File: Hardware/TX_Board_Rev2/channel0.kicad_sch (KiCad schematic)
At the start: 65 parts, among them IC15 PMA3-63GLN+, IC19 PE42423B-Z, IC23 PE42423B-Z, IC4 MAPS-010164-TR0500, IC5 QPA9122TR7, J3 MM8030-2610RJ3, J4 Conn_Coaxial, J5 Conn_Coaxial

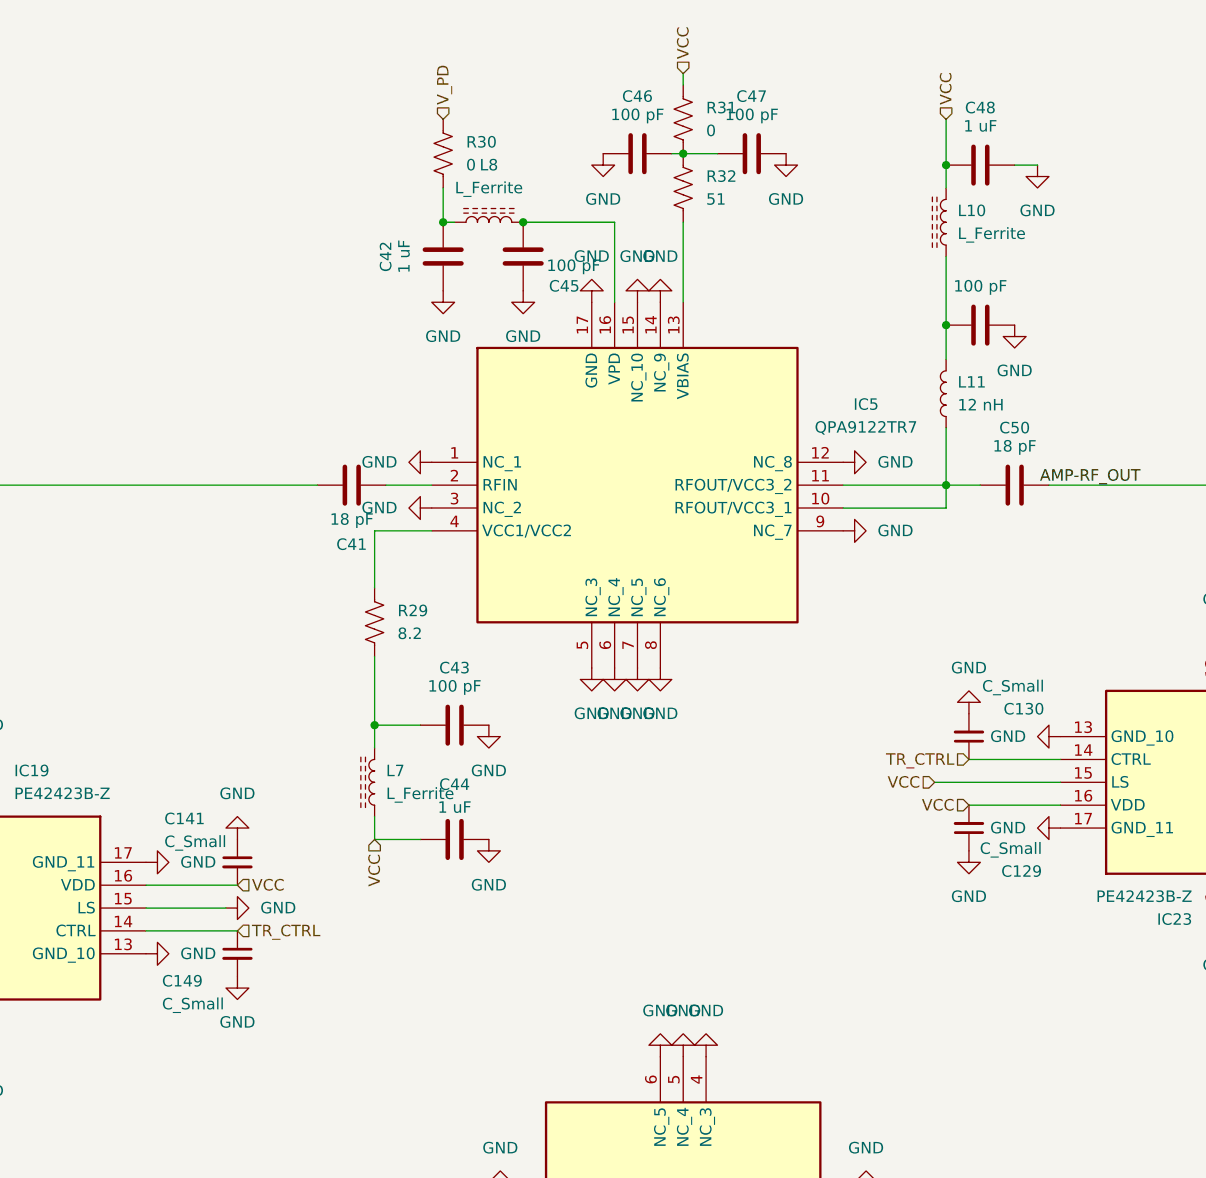
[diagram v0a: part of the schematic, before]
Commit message: Rev2 layout partially complete
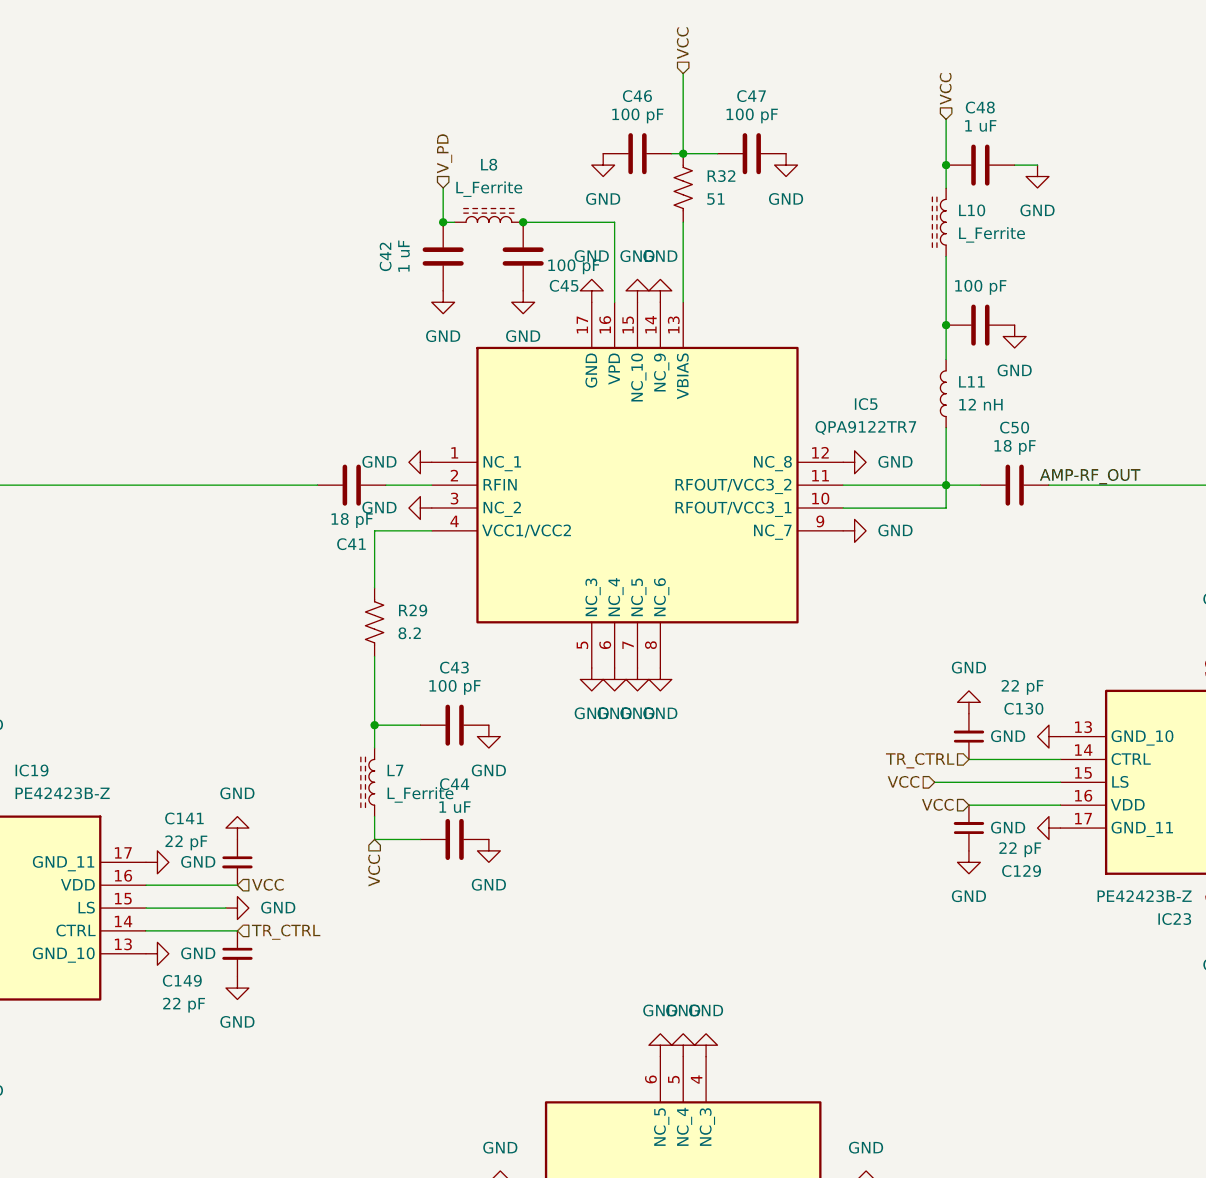
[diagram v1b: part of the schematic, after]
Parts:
- removed R30, R31: 0, Resistor_SMD:R_0603_1608Metric, symbol tx_board_symbol_library:R_US
- AT2: footprint tx_board_footprints:QFN50P300X300X90-17N -> RFSA3713:QFN50P300X300X90-17N
- C1, C10, C11, C12, C2, C3, C36, C37, C38, C39, C40, C42, C43, C44, C45, C46, C47, C48, C49, C6, C7, C8, C9: footprint Capacitor_SMD:C_0603_1608Metric -> Capacitor_SMD:C_0402_1005Metric
- C113, C116: footprint Capacitor_SMD:C_0402_1005Metric_Pad0.74x0.62mm_HandSolder -> Capacitor_SMD:C_0402_1005Metric
- C114: footprint Capacitor_SMD:C_1206_3216Metric_Pad1.33x1.80mm_HandSolder -> Capacitor_SMD:C_0402_1005Metric
- C115: footprint Capacitor_SMD:C_0603_1608Metric_Pad1.08x0.95mm_HandSolder -> Capacitor_SMD:C_0402_1005Metric
- C129, C130, C141, C149: value C_Small -> 22 pF; footprint (none) -> Capacitor_SMD:C_0402_1005Metric
- IC19, IC23: footprint PE42423B-Z:QFN50P300X300X90-17N-D -> PE42423:QFN50P300X300X90-17N-D
- IC4: footprint tx_board_footprints:QFN50P400X400X100-25N-D -> MAPS-010164-TR0500:QFN50P400X400X100-25N-D
- IC5: footprint tx_board_footprints:QPA9122TR7 -> QPA9122-TR7:QPA9122TR7
- J3: footprint tx_board_footprints:MM80302610RJ3 -> MM8030-2610RJ3:MM80302610RJ3
- R12, R13, R14, R15, R16, R17, R29, R32, R4: footprint Resistor_SMD:R_0603_1608Metric -> Resistor_SMD:R_0402_1005Metric
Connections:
- net VCC: now also C46.2, C47.1, R32.1
- net V_PD: now also C42.2, L8.1

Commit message: Rev2 Complete
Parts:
- removed J4: Conn_Coaxial, Connector_Coaxial:SMA_Samtec_SMA-J-P-H-ST-EM1_EdgeMount, symbol Connector:Conn_Coaxial
- added J1: CONSMA022-G, CONSMA022_G:LINX_CONSMA022-G, symbol CONSMA022-G:CONSMA022-G
- added R51, R52: 20k, Resistor_SMD:R_0402_1005Metric, symbol Device:R_US
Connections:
- net GND: now also J1.2, J1.3, J1.4, J1.5, R51.2; no longer IC19.15 (LS)
- net OUTPUT: now also J1.1
- net VCC: now also R52.1; no longer IC23.15 (LS)
- new net: IC23.15 (LS), R52.2
- new net: IC19.15 (LS), R51.1

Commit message: Rev 3, rotated interface connectors
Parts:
- renumbered AT2 to AT0, HY2 to CPL0, J5 to CPL_PORT0, J1 to J0, J3 to J8, IC15 to LNA0, IC5 to PA0, IC4 to PS0, IC19 to SW00, IC23 to SW01
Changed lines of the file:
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@@
 		(dnp no)
 		(fields_autoplaced yes)
-		(property "Reference" "J1"
+		(property "Reference" "J0"
 			(at 673.2905 262.89 0)
 			(effects
@@
 			(project ""
 				(path "/5327d041-dca0-47c6-802d-ce81714adf6c/7bb8dd1e-0839-4907-9be8-cd94b974a535"
-					(reference "J1")
+					(reference "J0")
 					(unit 1)
 				)
@@
 		(dnp no)
 		(fields_autoplaced yes)
-		(property "Reference" "IC23"
+		(property "Reference" "SW01"
 			(at 558.2219 266.7 90)
 			(effects
@@
 			(project "TX_Board_Rev2"
 				(path "/5327d041-dca0-47c6-802d-ce81714adf6c/7bb8dd1e-0839-4907-9be8-cd94b974a535"
-					(reference "IC23")
+					(reference "SW01")
 					(unit 1)
 				)
@@
 		(on_board yes)
 		(dnp no)
-		(property "Reference" "IC15"
+		(property "Reference" "LNA0"
 			(at 502.412 303.276 0)
 			(effects
@@
 			(project "TX_Board_Rev2"
 				(path "/5327d041-dca0-47c6-802d-ce81714adf6c/7bb8dd1e-0839-4907-9be8-cd94b974a535"
-					(reference "IC15")
+					(reference "LNA0")
 					(unit 1)
 				)
@@
 		(on_board yes)
 		(dnp no)
-		(property "Reference" "IC4"
+		(property "Reference" "PS0"
 			(at 250.19 248.8498 0)
 			(effects
@@
 			(project "TX_Board_Rev2"
 				(path "/5327d041-dca0-47c6-802d-ce81714adf6c/7bb8dd1e-0839-4907-9be8-cd94b974a535"
-					(reference "IC4")
+					(reference "PS0")
 					(unit 1)
 				)
@@
 		(on_board yes)
 		(dnp no)
-		(property "Reference" "J3"
+		(property "Reference" "J8"
 			(at 381.762 286.766 90)
 			(effects
@@
 			(project "TX_Board_Rev2"
 				(path "/5327d041-dca0-47c6-802d-ce81714adf6c/7bb8dd1e-0839-4907-9be8-cd94b974a535"
-					(reference "J3")
+					(reference "J8")
 					(unit 1)
 				)
@@
 		(dnp no)
 		(fields_autoplaced yes)
-		(property "Reference" "IC5"
+		(property "Reference" "PA0"
 			(at 521.97 209.4798 0)
 			(effects
@@
 			(project "TX_Board_Rev2"
 				(path "/5327d041-dca0-47c6-802d-ce81714adf6c/7bb8dd1e-0839-4907-9be8-cd94b974a535"
-					(reference "IC5")
+					(reference "PA0")
 					(unit 1)
 				)
@@
 		(dnp no)
 		(fields_autoplaced yes)
-		(property "Reference" "HY2"
+		(property "Reference" "CPL0"
 			(at 641.35 243.84 0)
 			(effects
@@
 			(project "TX_Board_Rev2"
 				(path "/5327d041-dca0-47c6-802d-ce81714adf6c/7bb8dd1e-0839-4907-9be8-cd94b974a535"
-					(reference "HY2")
+					(reference "CPL0")
 					(unit 1)
 				)
@@
 		(dnp no)
 		(fields_autoplaced yes)
-		(property "Reference" "IC19"
+		(property "Reference" "SW00"
 			(at 427.2981 250.19 90)
 			(effects
@@
 			(project "TX_Board_Rev2"
 				(path "/5327d041-dca0-47c6-802d-ce81714adf6c/7bb8dd1e-0839-4907-9be8-cd94b974a535"
-					(reference "IC19")
+					(reference "SW00")
 					(unit 1)
 				)
@@
 		(dnp no)
 		(fields_autoplaced yes)
-		(property "Reference" "J5"
+		(property "Reference" "CPL_PORT0"
 			(at 690.88 241.5931 0)
 			(effects
@@
 			(project "TX_Board_Rev2"
 				(path "/5327d041-dca0-47c6-802d-ce81714adf6c/7bb8dd1e-0839-4907-9be8-cd94b974a535"
-					(reference "J5")
+					(reference "CPL_PORT0")
 					(unit 1)
 				)
@@
 		(dnp no)
 		(fields_autoplaced yes)
-		(property "Reference" "AT2"
+		(property "Reference" "AT0"
 			(at 334.01 251.3898 0)
 			(effects
@@
 			(project "TX_Board_Rev2"
 				(path "/5327d041-dca0-47c6-802d-ce81714adf6c/7bb8dd1e-0839-4907-9be8-cd94b974a535"
-					(reference "AT2")
+					(reference "AT0")
 					(unit 1)
 				)

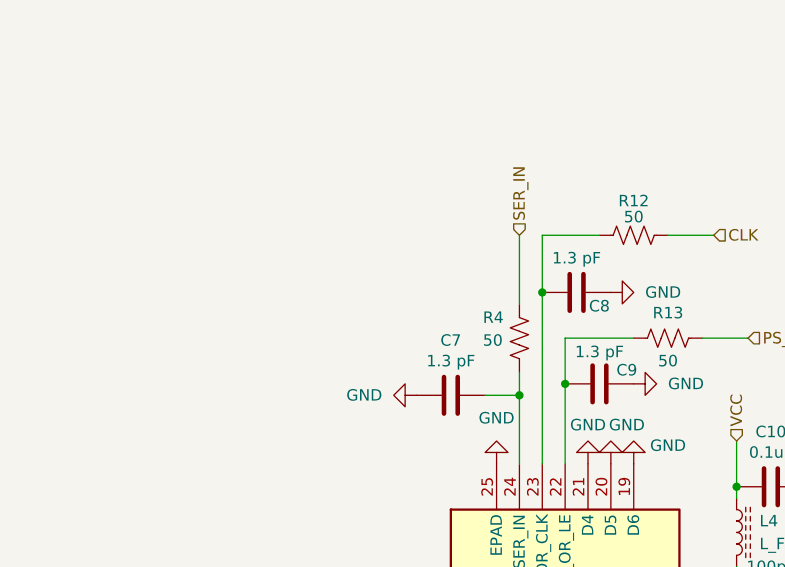
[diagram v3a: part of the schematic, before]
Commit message: optimal radiation patterns + a few rev 3 fixes
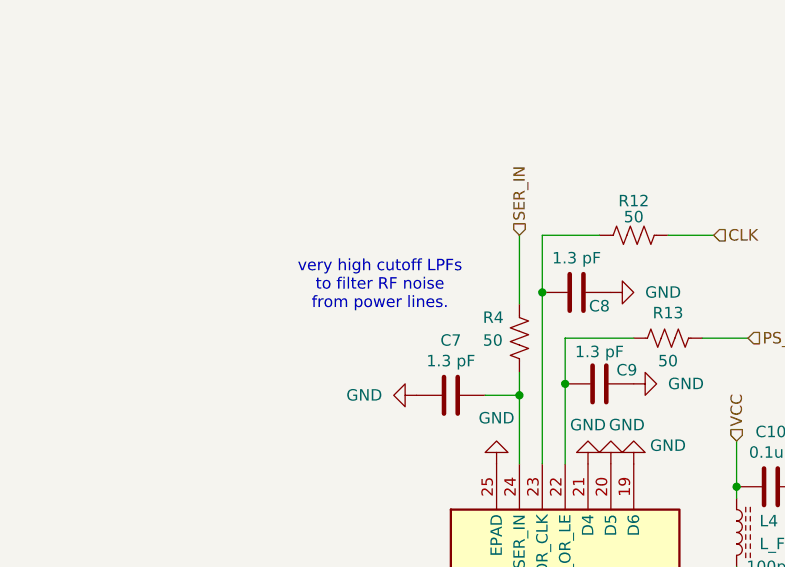
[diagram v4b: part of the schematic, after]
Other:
- note added: "very high cutoff LPFs to filter RF noise from power lines."
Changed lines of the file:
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@@
+		)
+	)
+	(text "very high cutoff LPFs \nto filter RF noise \nfrom power lines."
+		(exclude_from_sim no)
+		(at 206.756 210.058 0)
+		(effects
+			(font
+				(size 1.27 1.27)
+			)
 		)
 	)

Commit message: Restored broken Rev 2 for posterity and cleaned up naming
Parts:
- renumbered AT0 to AT2, CPL0 to HY2, LNA0 to IC15, SW00 to IC19, SW01 to IC23, PS0 to IC4, PA0 to IC5, J0 to J1, J8 to J3, CPL_PORT0 to J5
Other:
- note removed: "very high cutoff LPFs to filter RF noise from power lines."
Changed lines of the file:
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@@
 		)
 	)
-	(text "very high cutoff LPFs \nto filter RF noise \nfrom power lines."
-		(exclude_from_sim no)
-		(at 206.756 210.058 0)
-		(effects
-			(font
-				(size 1.27 1.27)
-			)
-		)
-	)
 	(junction
 		(at 191.77 255.27)
@@
 		(dnp no)
 		(fields_autoplaced yes)
-		(property "Reference" "J0"
+		(property "Reference" "J1"
 			(at 673.2905 262.89 0)
 			(effects
@@
 			(project ""
 				(path "/5327d041-dca0-47c6-802d-ce81714adf6c/7bb8dd1e-0839-4907-9be8-cd94b974a535"
-					(reference "J0")
+					(reference "J1")
 					(unit 1)
 				)
@@
 		(dnp no)
 		(fields_autoplaced yes)
-		(property "Reference" "SW01"
+		(property "Reference" "IC23"
 			(at 558.2219 266.7 90)
 			(effects
@@
 			(project "TX_Board_Rev2"
 				(path "/5327d041-dca0-47c6-802d-ce81714adf6c/7bb8dd1e-0839-4907-9be8-cd94b974a535"
-					(reference "SW01")
+					(reference "IC23")
 					(unit 1)
 				)
@@
 		(on_board yes)
 		(dnp no)
-		(property "Reference" "LNA0"
+		(property "Reference" "IC15"
 			(at 502.412 303.276 0)
 			(effects
@@
 			(project "TX_Board_Rev2"
 				(path "/5327d041-dca0-47c6-802d-ce81714adf6c/7bb8dd1e-0839-4907-9be8-cd94b974a535"
-					(reference "LNA0")
+					(reference "IC15")
 					(unit 1)
 				)
@@
 		(on_board yes)
 		(dnp no)
-		(property "Reference" "PS0"
+		(property "Reference" "IC4"
 			(at 250.19 248.8498 0)
 			(effects
@@
 			(project "TX_Board_Rev2"
 				(path "/5327d041-dca0-47c6-802d-ce81714adf6c/7bb8dd1e-0839-4907-9be8-cd94b974a535"
-					(reference "PS0")
+					(reference "IC4")
 					(unit 1)
 				)
@@
 		(on_board yes)
 		(dnp no)
-		(property "Reference" "J8"
+		(property "Reference" "J3"
 			(at 381.762 286.766 90)
 			(effects
@@
 			(project "TX_Board_Rev2"
 				(path "/5327d041-dca0-47c6-802d-ce81714adf6c/7bb8dd1e-0839-4907-9be8-cd94b974a535"
-					(reference "J8")
+					(reference "J3")
 					(unit 1)
 				)
@@
 		(dnp no)
 		(fields_autoplaced yes)
-		(property "Reference" "PA0"
+		(property "Reference" "IC5"
 			(at 521.97 209.4798 0)
 			(effects
@@
 			(project "TX_Board_Rev2"
 				(path "/5327d041-dca0-47c6-802d-ce81714adf6c/7bb8dd1e-0839-4907-9be8-cd94b974a535"
-					(reference "PA0")
+					(reference "IC5")
 					(unit 1)
 				)
@@
 		(dnp no)
 		(fields_autoplaced yes)
-		(property "Reference" "CPL0"
+		(property "Reference" "HY2"
 			(at 641.35 243.84 0)
 			(effects
@@
 			(project "TX_Board_Rev2"
 				(path "/5327d041-dca0-47c6-802d-ce81714adf6c/7bb8dd1e-0839-4907-9be8-cd94b974a535"
-					(reference "CPL0")
+					(reference "HY2")
 					(unit 1)
 				)
@@
 		(dnp no)
 		(fields_autoplaced yes)
-		(property "Reference" "SW00"
+		(property "Reference" "IC19"
 			(at 427.2981 250.19 90)
 			(effects
@@
 			(project "TX_Board_Rev2"
 				(path "/5327d041-dca0-47c6-802d-ce81714adf6c/7bb8dd1e-0839-4907-9be8-cd94b974a535"
-					(reference "SW00")
+					(reference "IC19")
 					(unit 1)
 				)
@@
 		(dnp no)
 		(fields_autoplaced yes)
-		(property "Reference" "CPL_PORT0"
+		(property "Reference" "J5"
 			(at 690.88 241.5931 0)
 			(effects
@@
 			(project "TX_Board_Rev2"
 				(path "/5327d041-dca0-47c6-802d-ce81714adf6c/7bb8dd1e-0839-4907-9be8-cd94b974a535"
-					(reference "CPL_PORT0")
+					(reference "J5")
 					(unit 1)
 				)
@@
 		(dnp no)
 		(fields_autoplaced yes)
-		(property "Reference" "AT0"
+		(property "Reference" "AT2"
 			(at 334.01 251.3898 0)
 			(effects
@@
 			(project "TX_Board_Rev2"
 				(path "/5327d041-dca0-47c6-802d-ce81714adf6c/7bb8dd1e-0839-4907-9be8-cd94b974a535"
-					(reference "AT0")
+					(reference "AT2")
 					(unit 1)
 				)
